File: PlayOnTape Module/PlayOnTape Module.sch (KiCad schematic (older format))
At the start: 27 parts, among them IC1 0.96_OLED, J1 INPUT, J2 DATASETTE, J3 EXTENSION, J5 PWR, J6 N/C, M1 Mounting, M2 Mounting, M3 Mounting, M4 Mounting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

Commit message: Gerber export
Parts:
- D2: value RECEIVE -> RECORD
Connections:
- net RECEIVE renamed RECORD
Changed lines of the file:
@@
 P 12650 8200
 F 0 "D2" H 12600 8325 50  0000 L CNN
-F 1 "RECEIVE" H 12525 8125 50  0000 L CNN
+F 1 "RECORD" H 12525 8125 50  0000 L CNN
 F 2 "LED_THT:LED_D5.0mm" V 12650 8200 50  0001 C CNN
 F 3 "" V 12650 8200 50  0001 C CNN
@@
 	12825 8200 12825 8300
 Text GLabel 8700 3325 0    60   Output ~ 0
-RECEIVE
+RECORD
 Wire Wire Line
 	8700 3325 8775 3325
 Text GLabel 12075 8200 0    60   Input ~ 0
-RECEIVE
+RECORD
 Wire Wire Line
 	12075 8200 12150 8200

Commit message: Tweak input mounting holes
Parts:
- JP2: value P1_VCC -> P2_VCC
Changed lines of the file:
@@
 P 6050 7925
 F 0 "JP2" V 6004 7993 50  0000 L CNN
-F 1 "P1_VCC" V 6095 7993 50  0000 L CNN
+F 1 "P2_VCC" V 6095 7993 50  0000 L CNN
 F 2 "Jumper:SolderJumper-3_P1.3mm_Open_RoundedPad1.0x1.5mm" H 6050 7925 50  0001 C CNN
 F 3 "~" H 6050 7925 50  0001 C CNN

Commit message: Changed to use IDC cable
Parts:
- removed J6: N/C, Pin_Headers:Pin_Header_Straight_1x03_Pitch2.54mm, symbol Connector_Generic:Conn_01x03
- J1: footprint PlayOnTape:C64-Cassette-Input -> Connector_IDC:IDC-Header_2x03_P2.54mm_Vertical; symbol c64_cassette:C64_Cassette_Input -> c64_cassette:C64_Cassette_IDC
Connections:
- net +5V: now also R2.2
- net GND: no longer D2.1 (K)
- net RECORD: now also D2.1 (K); no longer R2.2
- no-connect marks 21 -> 18
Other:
- moved on the sheet: A1, D1, D2, J2, R1, R2, R6, SW1, SW2, SW3, SW4, U1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

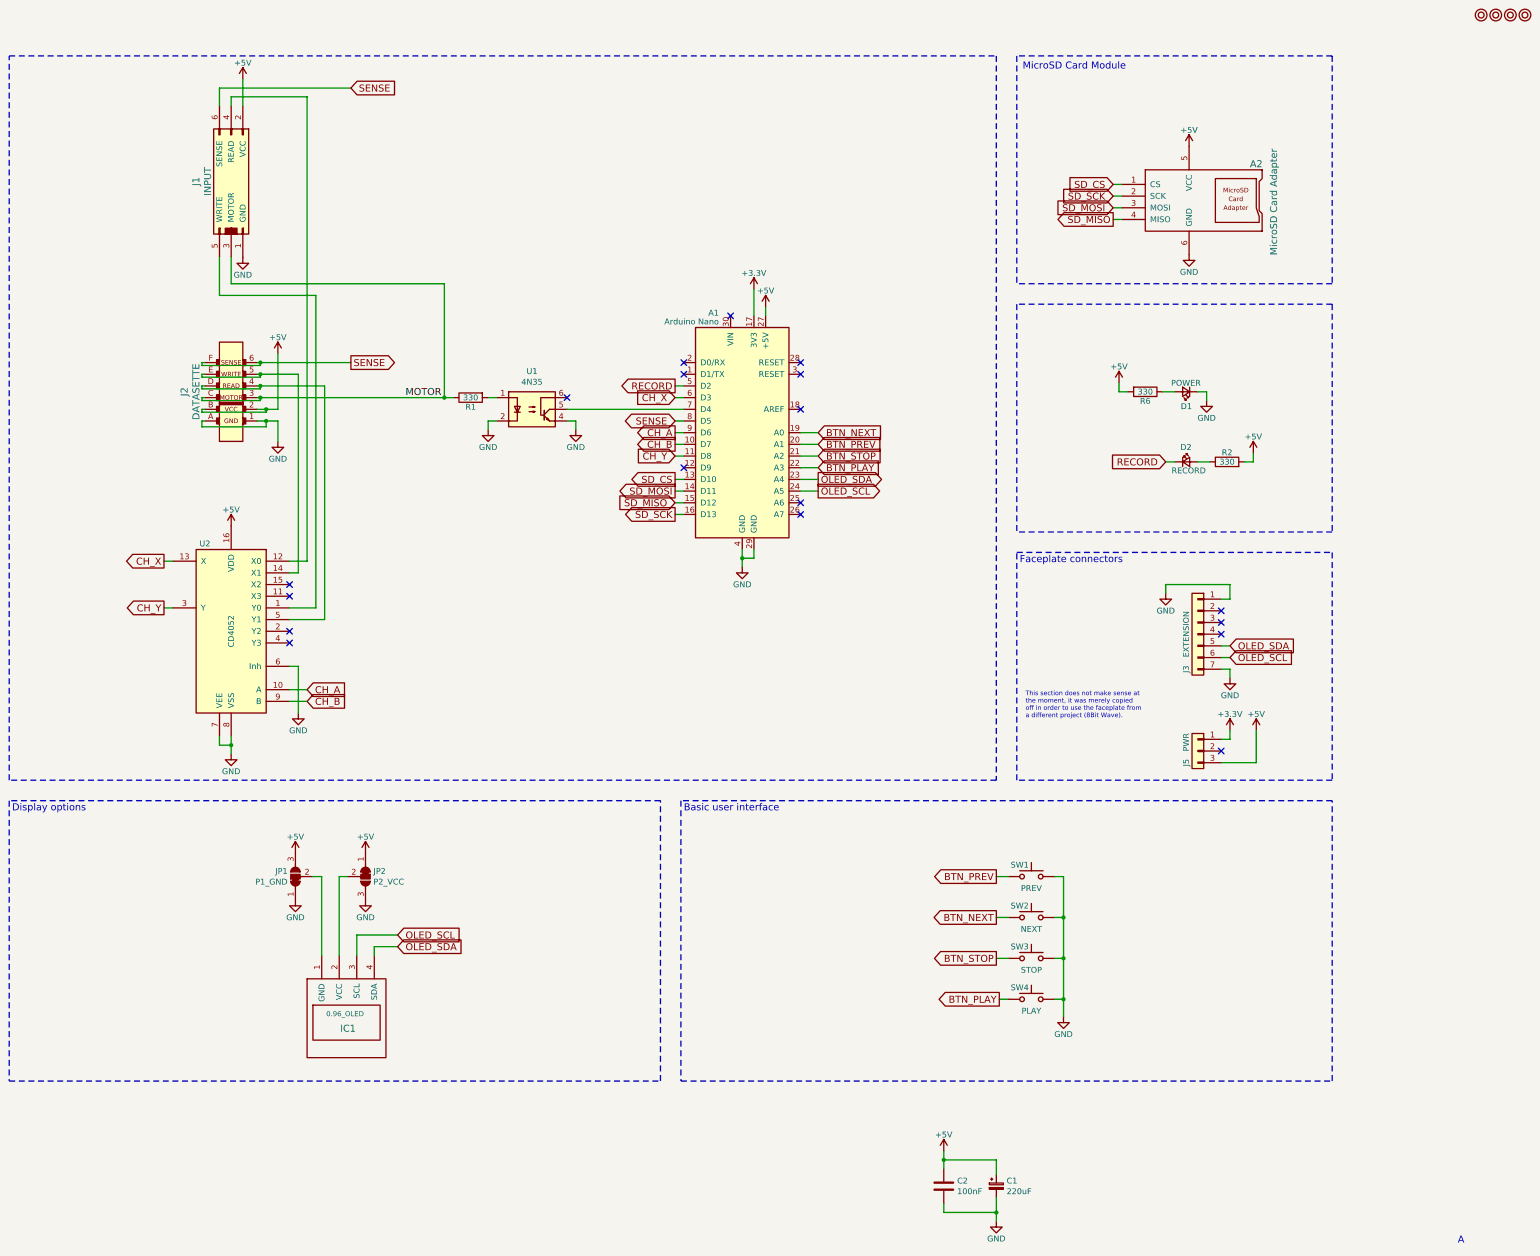
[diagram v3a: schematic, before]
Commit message: Some build instructions added
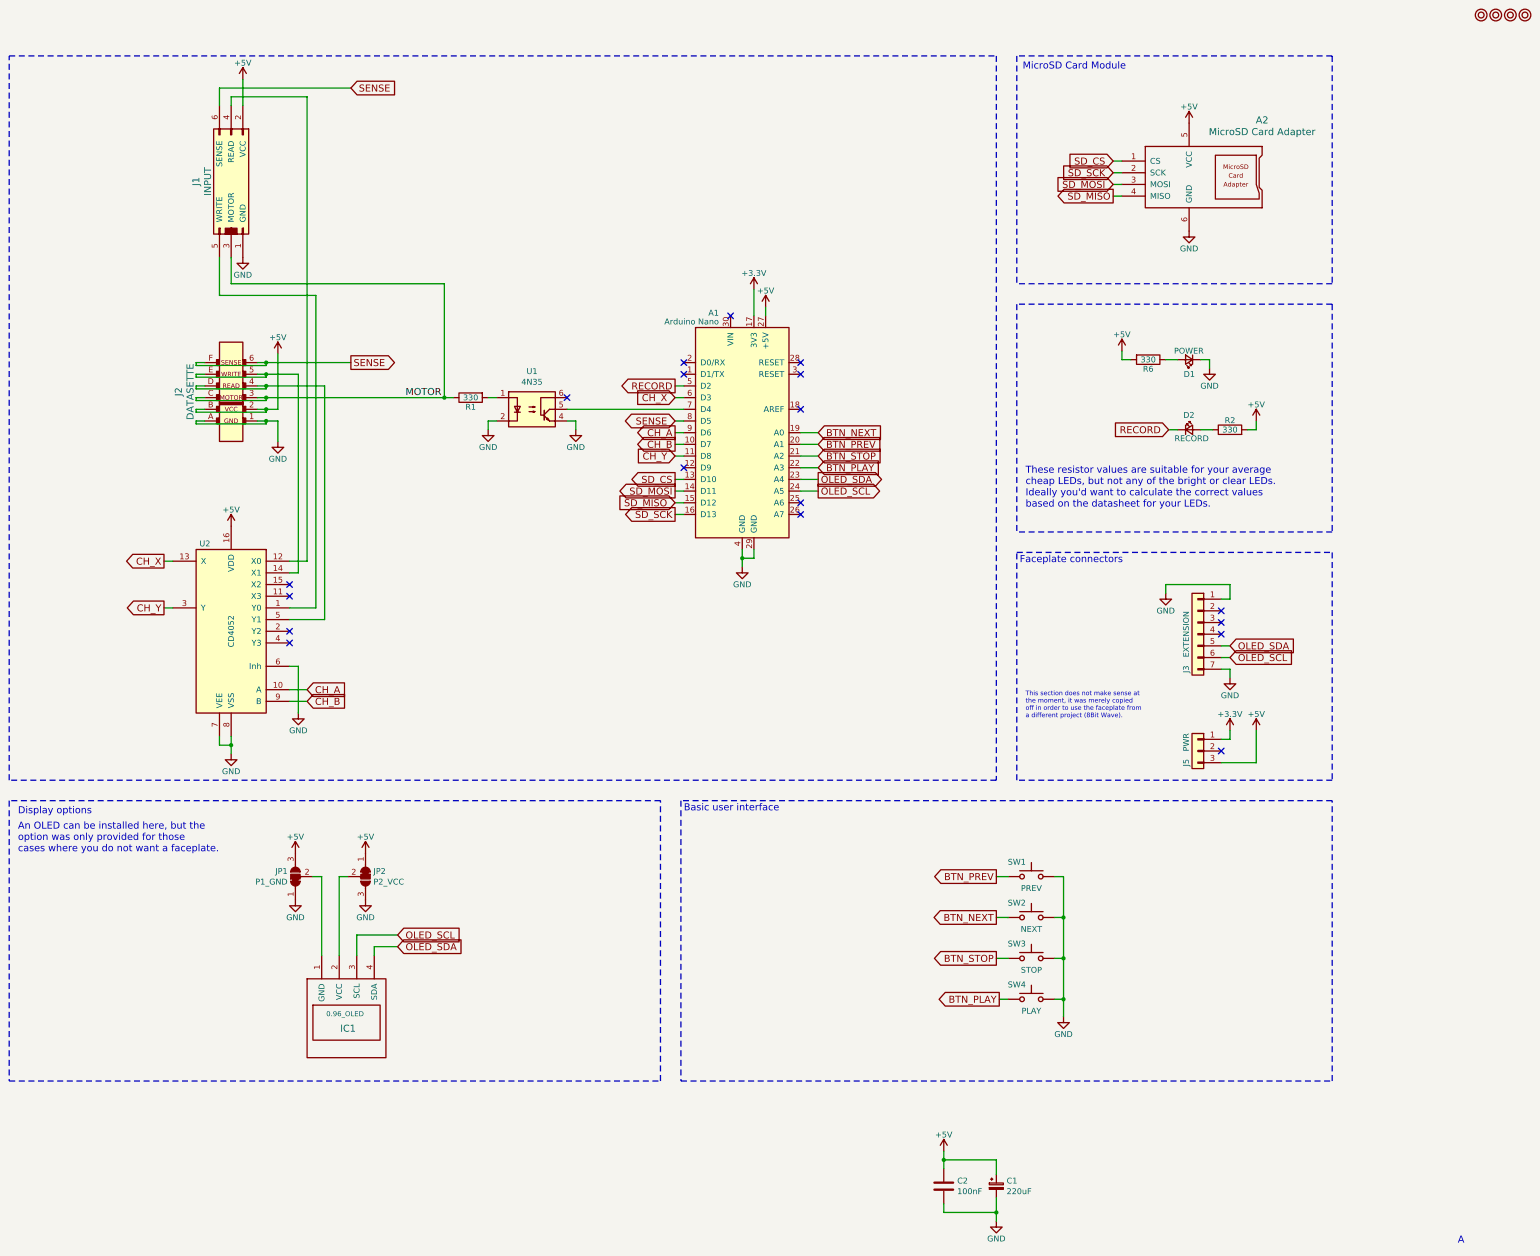
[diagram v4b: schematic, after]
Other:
- note added: "An OLED can be installed here, but the\noption was only provided for those\ncases where you do not want a faceplate."
- note added: "These resistor values are suitable for your average\ncheap LEDs, but not any of the bright or clear LEDs.\nIdeally you'd want to calculate the correct values\nbased on the datasheet for your LEDs."
- moved on the sheet: A2, D1, D2, R2, R6
